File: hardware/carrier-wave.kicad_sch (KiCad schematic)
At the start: 19 parts, among them J1 USB C 2.0, U1 STM32G0B1CBTx, U2 OPA695, U3 THS3491, U4 AD9834, U7 TS5A3159ADCK

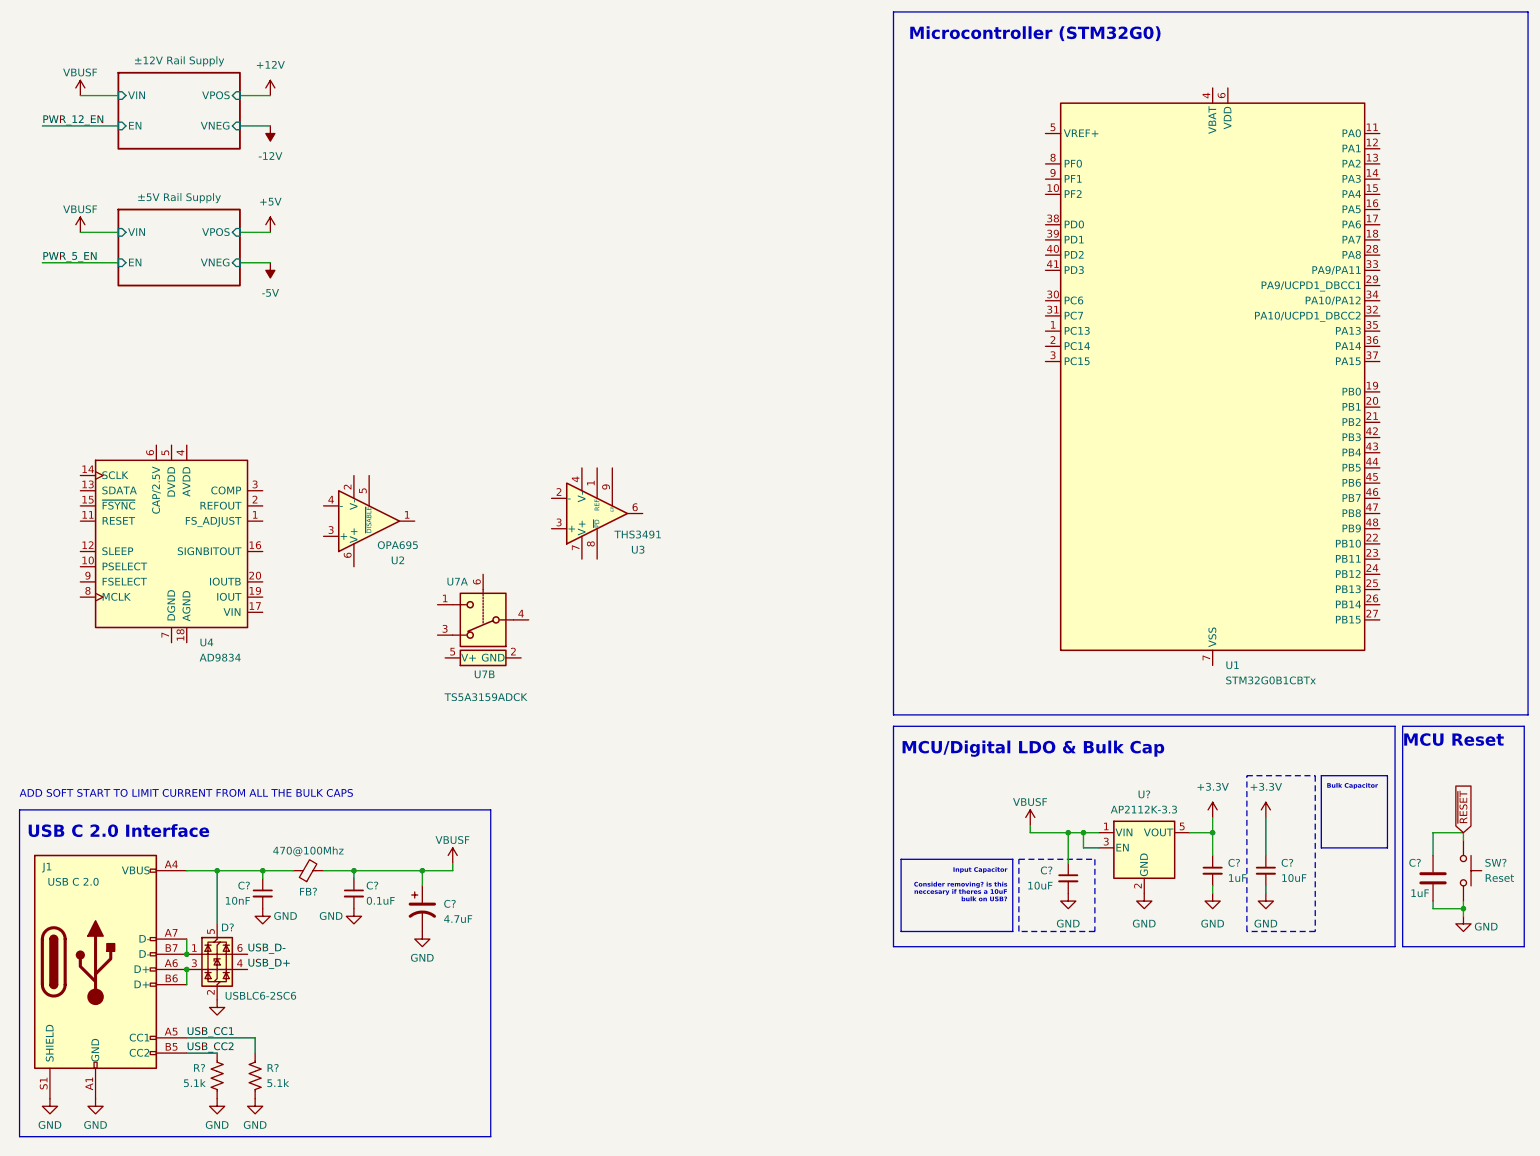
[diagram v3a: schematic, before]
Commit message: Add USB sheet and remove old components
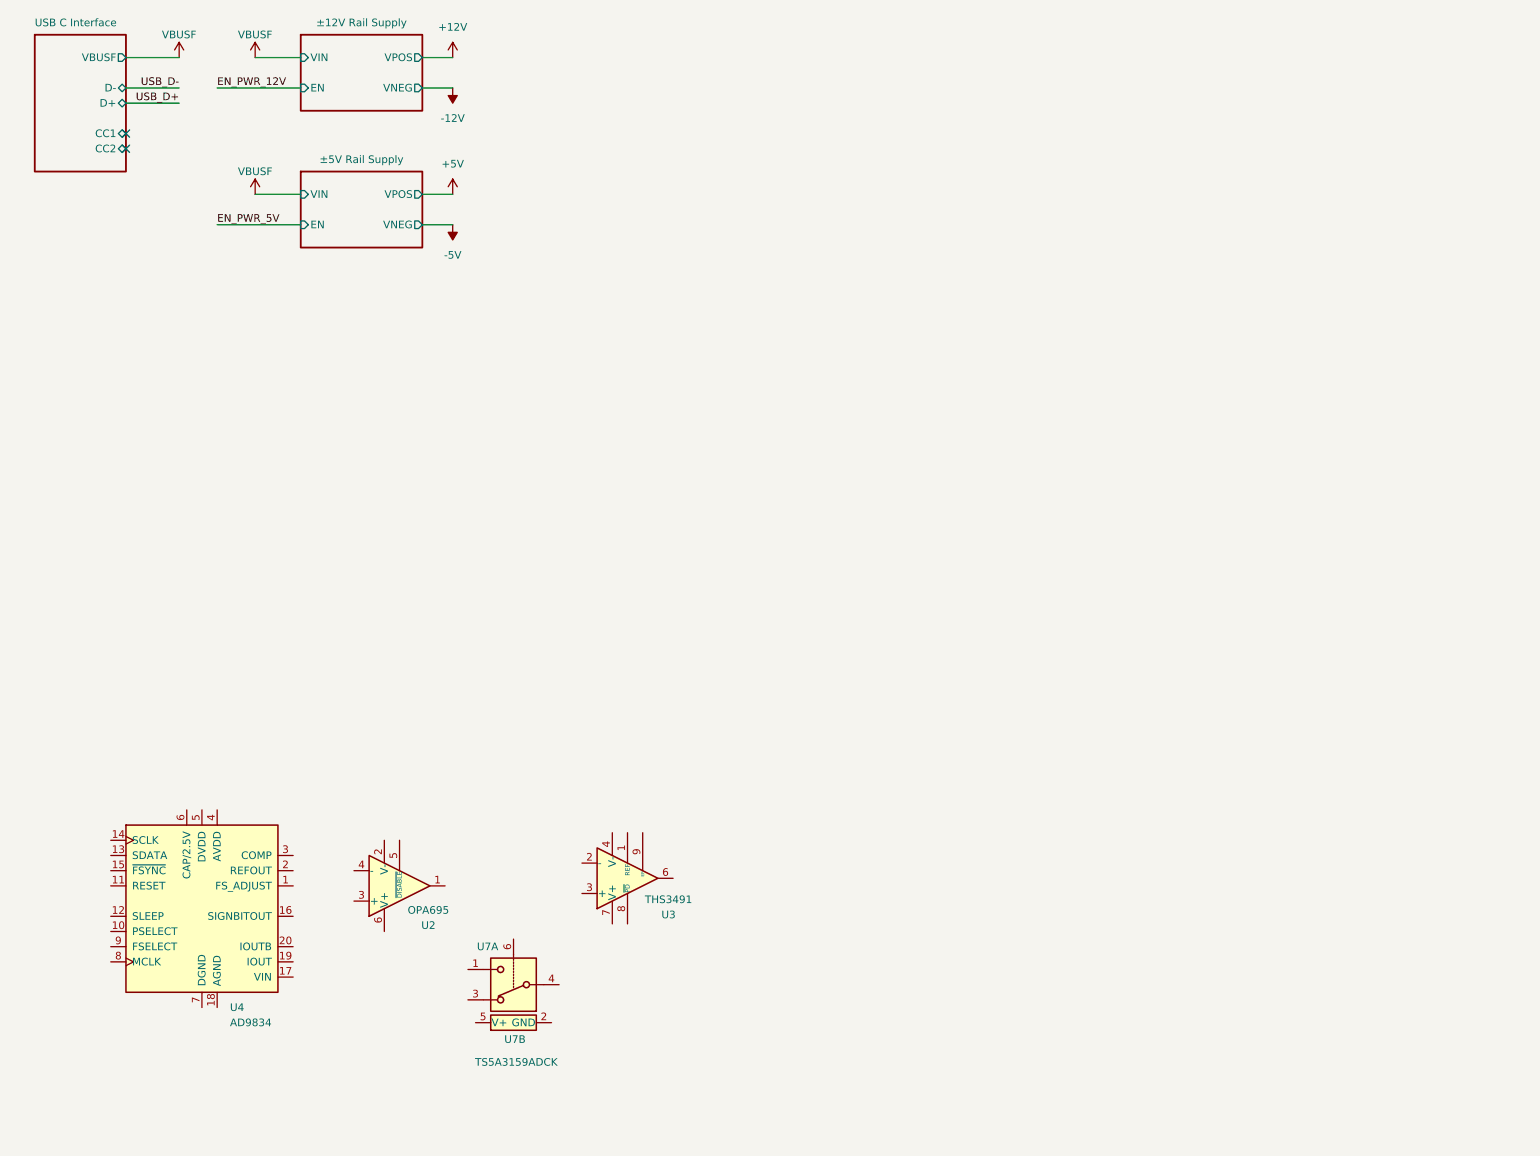
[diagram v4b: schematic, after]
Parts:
- removed C?: 1uF, Capacitor_SMD:C_0805_2012Metric_Pad1.18x1.45mm_HandSolder, symbol Device:C
- removed C? (x2): 10uF, symbol Device:C_Small
- removed C?: 0.1uF, symbol Device:C_Small
- removed C?: 4.7uF, HIGHER ESR ELECTROLYTIC, symbol Device:C_Polarized_US
- removed C?: 10nF, symbol Device:C_Small
- removed C?: 1uF, symbol Device:C_Small
- removed D?: USBLC6-2SC6, Package_TO_SOT_SMD:SOT-23-6_Handsoldering, symbol Power_Protection:USBLC6-2SC6
- removed FB?: 470@100Mhz, Inductor_SMD:L_0603_1608Metric_Pad1.05x0.95mm_HandSolder, symbol Device:FerriteBead_Small
- removed J1: USB C 2.0, Connector_USB:USB_C_Receptacle_G-Switch_GT-USB-7010ASV, symbol Connector:USB_C_Receptacle_USB2.0_14P
- removed R? (x2): 5.1k, symbol Device:R_US
- removed SW?: Reset, Button_Switch_SMD:SW_SPST_PTS810, symbol Switch:SW_Push
- removed U1: STM32G0B1CBTx, Package_QFP:LQFP-48_7x7mm_P0.5mm, symbol MCU_ST_STM32G0:STM32G0B1CBTx
- removed U?: AP2112K-3.3, Package_TO_SOT_SMD:SOT-23-5, symbol Regulator_Linear:AP2112K-3.3
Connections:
- no-connect marks 0 -> 2
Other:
- added sheet USB C Interface (usb_interface.kicad_sch)
- note removed: "ADD SOFT START TO LIMIT CURRENT FROM ALL THE BULK CAPS"
- note removed: "Bulk Capacitor"
- note removed: "Input Capacitor Consider removing? is this neccesary if theres a 10uF bulk on USB?"
- note removed: "MCU Reset"
- note removed: "MCU/Digital LDO & Bulk Cap"
- note removed: "Microcontroller (STM32G0)"
- note removed: "USB C 2.0 Interface"
- moved on the sheet: U2, U3, U4, U7A, U7B

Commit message: Finalize 5V rails
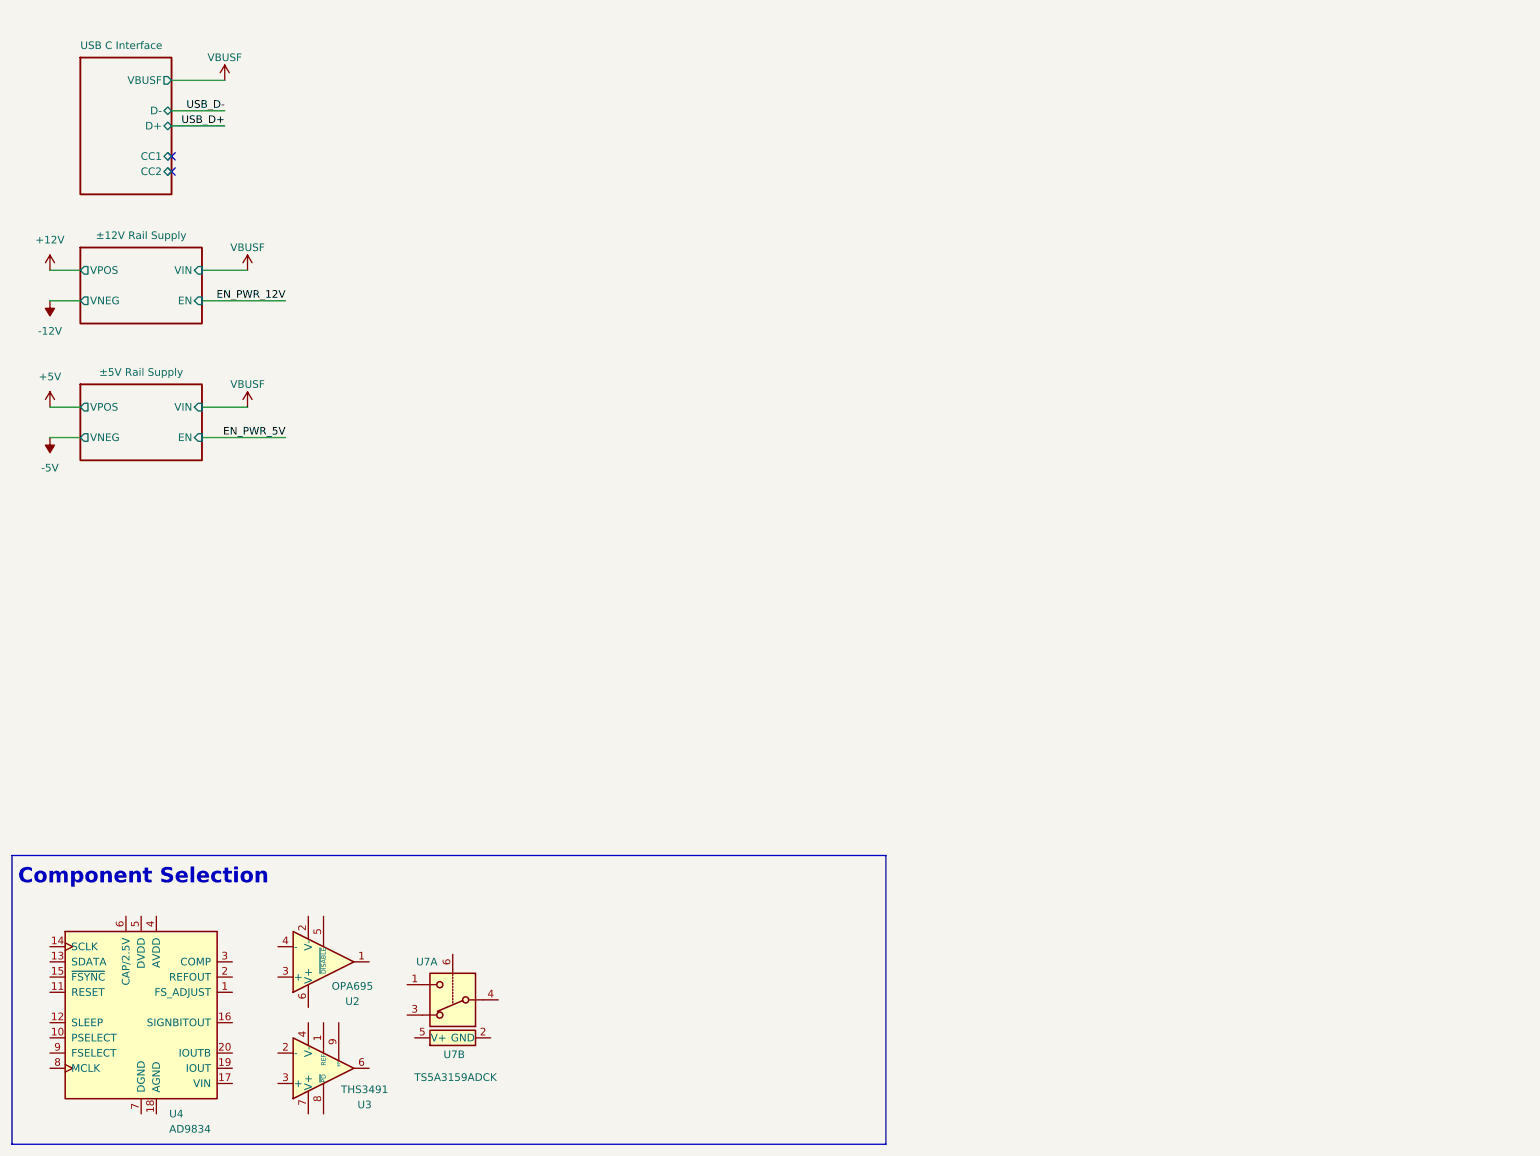
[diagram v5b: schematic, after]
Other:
- note added: "Component Selection"
- moved on the sheet: U2, U3, U4, U7A, U7B

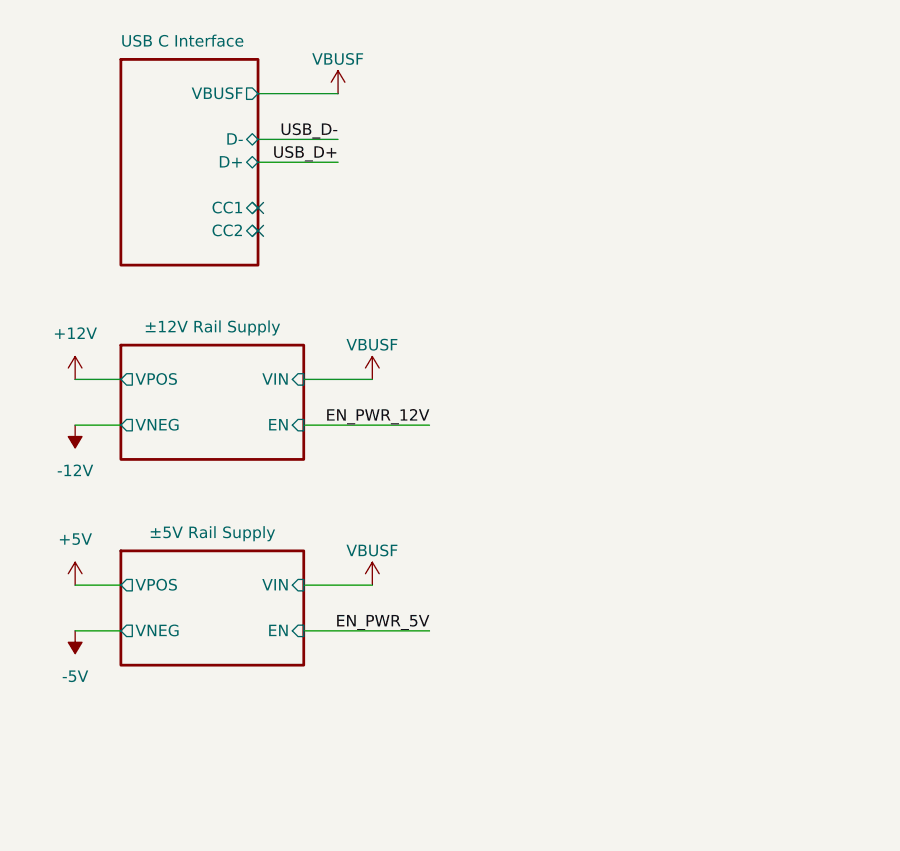
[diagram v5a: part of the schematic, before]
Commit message: Finalize USB interface
Added soft-start
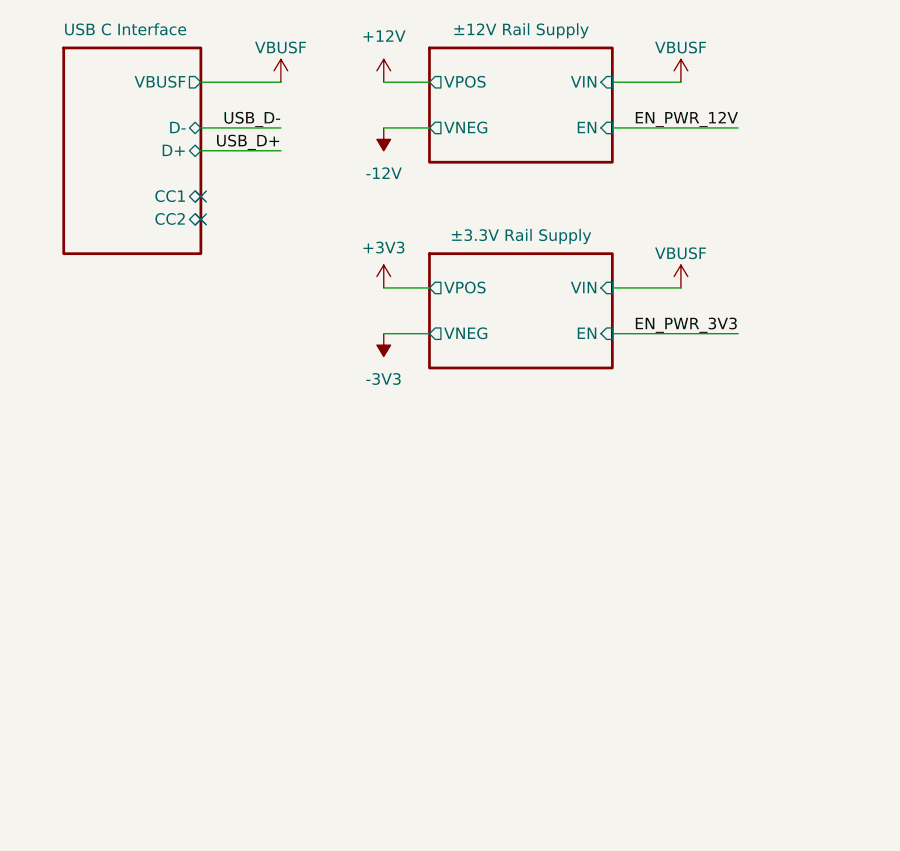
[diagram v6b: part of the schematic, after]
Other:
- sheet ±5V Rail Supply renamed ±3.3V Rail Supply
